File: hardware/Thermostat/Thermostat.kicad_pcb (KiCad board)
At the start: 2 copper layers, 111.2 x 76.5 mm, 47 parts, among them J1 Barrel_Jack_Switch, J2 Conn_01x02_Pin, J3 AVR-ISP-6, J4 MainConnectorr, K1 G6E, K2 G6E, K3 G6E, K4 G6E, SW1 12MM, SW2 12MM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

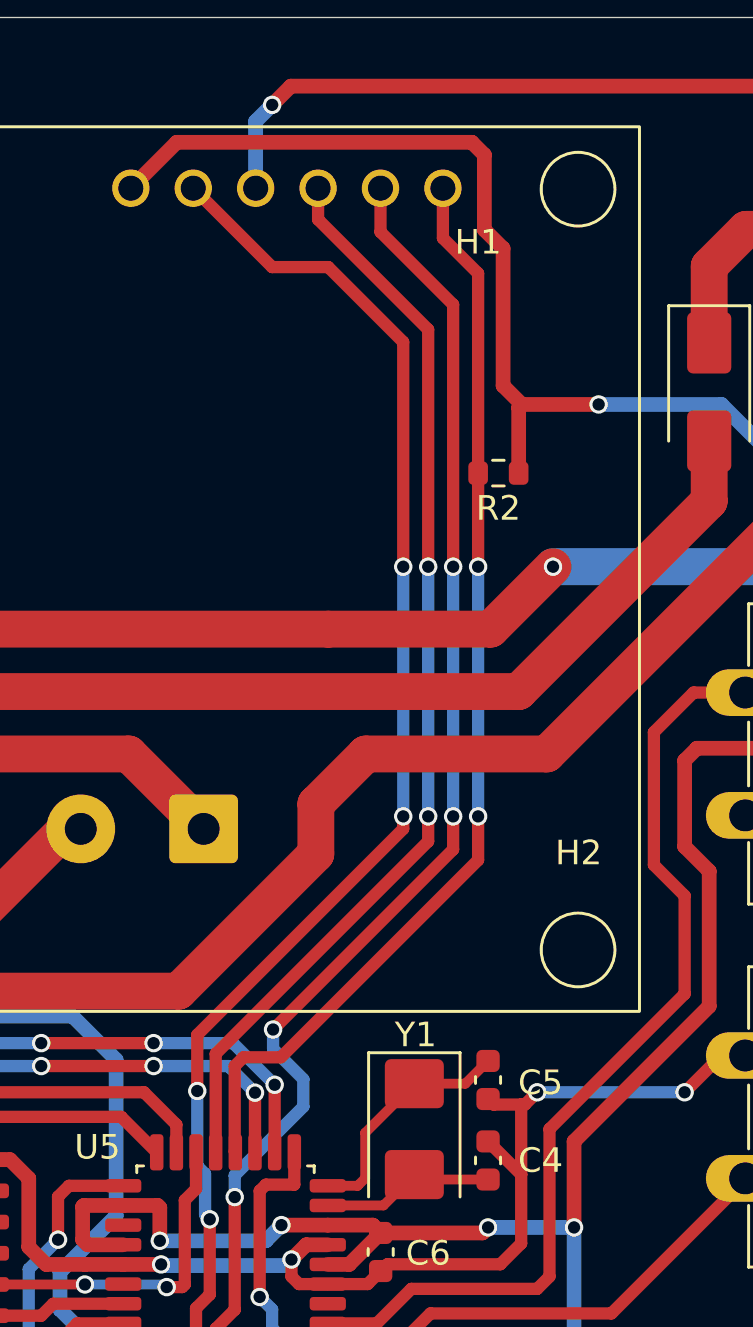
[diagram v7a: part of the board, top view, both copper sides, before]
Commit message: Put switches in order and move resistor
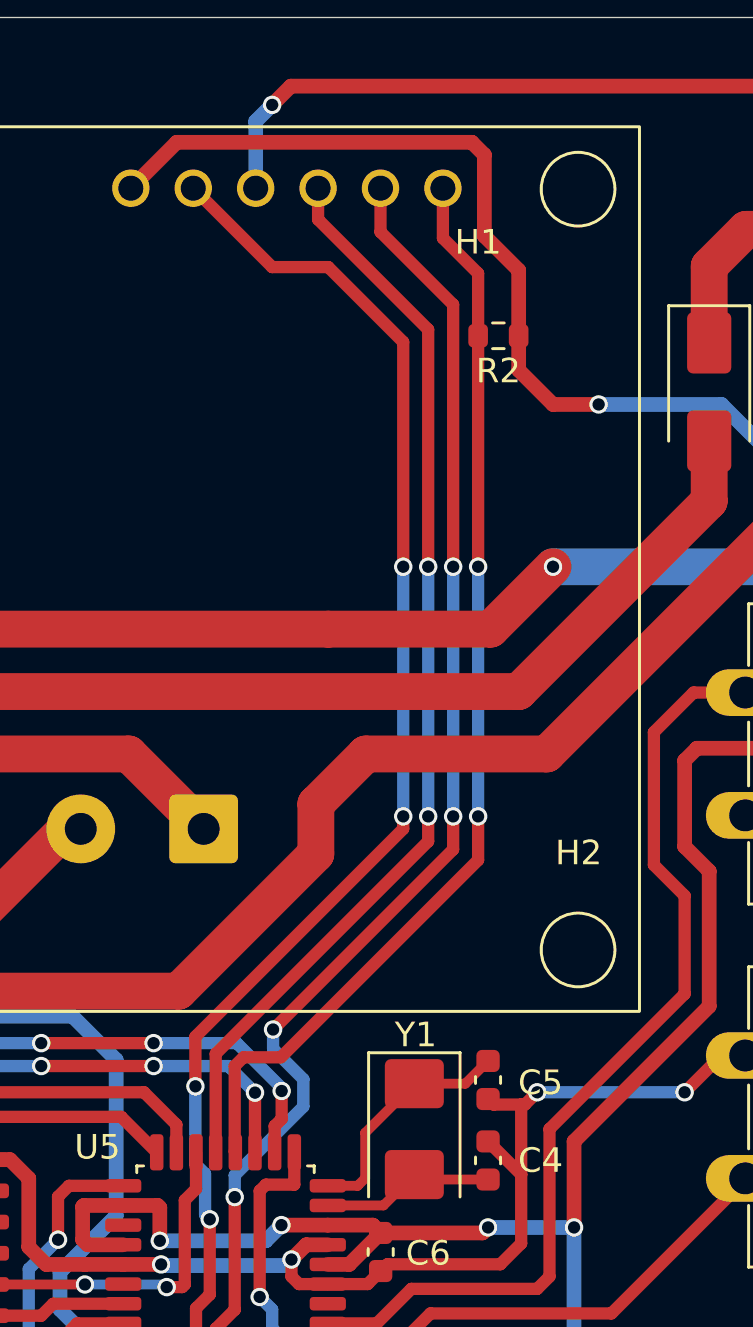
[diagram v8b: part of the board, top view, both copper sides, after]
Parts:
- moved R2 5.59 mm to (197.4, 61.2)
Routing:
- net +5V: track 206.4 -> 202.8 mm
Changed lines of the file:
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@@
 	(footprint "Resistor_SMD:R_0603_1608Metric"
 		(layer "F.Cu")
-		(at 197.421 66.802 180)
+		(at 197.421 61.214 180)
 		(descr "Resistor SMD 0603 (1608 Metric), square (rectangular) end terminal, IPC-7351 nominal, (Body size source: IPC-SM-782 page 72, https://www.pcb-3d.com/wordpress/wp-content/uploads/ipc-sm-782a_amendment_1_and_2.pdf), generated with kicad-footprint-generator")
 		(tags "resistor")
@@
 	)
 	(segment
+		(start 199.644 64.008)
+		(end 201.5 64.008)
+		(width 0.6)
+		(layer "F.Cu")
+		(net 3)
+	)
+	(segment
 		(start 188.5919 97.4059)
 		(end 190.4781 97.4059)
@@
 	)
 	(segment
-		(start 198.246 66.802)
-		(end 198.246 64.136)
-		(width 0.6)
-		(layer "F.Cu")
-		(net 3)
-	)
-	(segment
 		(start 182.1531 98.2059)
 		(end 180.7059 98.2059)
@@
 	)
 	(segment
-		(start 200.5 94)
-		(end 206 88.5)
+		(start 196.85 53.848)
+		(end 196.85 57.15)
 		(width 0.6)
 		(layer "F.Cu")
@@
 	)
 	(segment
-		(start 196.85 53.848)
-		(end 196.85 56.896)
+		(start 200.5 94)
+		(end 206 88.5)
 		(width 0.6)
 		(layer "F.Cu")
@@
 	)
 	(segment
-		(start 197.612 57.658)
-		(end 197.612 63.246)
+		(start 182.463 55.207)
+		(end 184.33 53.34)
 		(width 0.6)
 		(layer "F.Cu")
@@
 	)
 	(segment
+		(start 184.33 53.34)
+		(end 196.342 53.34)
+		(width 0.6)
+		(layer "F.Cu")
+		(net 3)
+	)
+	(segment
 		(start 180.5 96.6559)
 		(end 180.55 96.6059)
@@
 	)
 	(segment
+		(start 196.85 57.15)
+		(end 198.246 58.546)
+		(width 0.6)
+		(layer "F.Cu")
+		(net 3)
+	)
+	(segment
 		(start 190 107.5)
 		(end 191.5 107.5)
@@
 	)
 	(segment
-		(start 211.793 75.989)
-		(end 211.793 68.072)
+		(start 198.246 58.546)
+		(end 198.246 62.61)
 		(width 0.6)
 		(layer "F.Cu")
@@
 	)
 	(segment
-		(start 198.374 64.008)
-		(end 201.5 64.008)
+		(start 211.793 75.989)
+		(end 211.793 68.072)
 		(width 0.6)
 		(layer "F.Cu")
@@
 	)
 	(segment
-		(start 182.463 55.207)
-		(end 184.33 53.34)
-		(width 0.6)
-		(layer "F.Cu")
-		(net 3)
-	)
-	(segment
 		(start 200.5 97.5)
 		(end 200.5 94)
@@
 	)
 	(segment
-		(start 198.246 64.136)
-		(end 198.374 64.008)
-		(width 0.6)
-		(layer "F.Cu")
-		(net 3)
-	)
-	(segment
 		(start 189.5 116.5)
 		(end 191 116.5)
@@
 	)
 	(segment
-		(start 196.85 56.896)
-		(end 197.612 57.658)
-		(width 0.6)
-		(layer "F.Cu")
-		(net 3)
-	)
-	(segment
 		(start 205 82)
 		(end 205 78.5)
@@
 	)
 	(segment
-		(start 197.612 63.246)
-		(end 198.374 64.008)
-		(width 0.6)
-		(layer "F.Cu")
-		(net 3)
-	)
-	(segment
 		(start 209.782 78)
 		(end 211.793 75.989)
@@
 	)
 	(segment
-		(start 184.33 53.34)
-		(end 196.342 53.34)
+		(start 198.246 62.61)
+		(end 199.644 64.008)
 		(width 0.6)
 		(layer "F.Cu")
@@
 	)
 	(segment
+		(start 185.0906 91.757)
+		(end 185.0906 89.7374)
+		(width 0.5)
+		(layer "F.Cu")
+		(net 20)
+	)
+	(segment
 		(start 185.1156 100.791036)
 		(end 185.1156 102.7684)
@@
 	)
 	(segment
+		(start 193.548 81.28)
+		(end 193.548 80.772)
+		(width 0.5)
+		(layer "F.Cu")
+		(net 20)
+	)
+	(segment
 		(start 191.845 110.595)
 		(end 193.75 112.5)
@@
 	)
 	(segment
-		(start 185.1656 89.6624)
-		(end 185.1656 91.948)
-		(width 0.5)
-		(layer "F.Cu")
-		(net 20)
-	)
-	(segment
-		(start 193.548 80.772)
-		(end 193.548 81.28)
-		(width 0.5)
-		(layer "F.Cu")
-		(net 20)
-	)
-	(segment
 		(start 185.1156 105.9684)
 		(end 185.1156 102.7684)
@@
 	)
 	(segment
-		(start 184.912 106.172)
-		(end 185.1156 105.9684)
+		(start 185.0906 89.7374)
+		(end 193.548 81.28)
 		(width 0.5)
 		(layer "F.Cu")
@@
 	)
 	(segment
-		(start 185.166 91.9476)
-		(end 185.1656 91.948)
+		(start 184.912 106.172)
+		(end 185.1156 105.9684)
 		(width 0.5)
 		(layer "F.Cu")
@@
 		(net 20)
 	)
-	(segment
-		(start 193.548 81.28)
-		(end 185.1656 89.6624)
-		(width 0.5)
-		(layer "F.Cu")
-		(net 20)
-	)
 	(via
 		(at 190.5 109)
@@
 	)
 	(via
-		(at 185.1656 91.948)
+		(at 185.0906 91.757)
 		(size 0.75)
 		(drill 0.5)
@@
 	)
 	(segment
-		(start 185.1656 94.9956)
-		(end 185.1656 91.948)
+		(start 185.0906 94.9206)
+		(end 185.0906 91.757)
 		(width 0.5)
 		(layer "B.Cu")
@@
 	)
 	(segment
+		(start 185.483 96.978)
+		(end 185.483 95.313)
+		(width 0.5)
+		(layer "B.Cu")
+		(net 20)
+	)
+	(segment
 		(start 184.912 106.172)
 		(end 186.172 106.172)
@@
 	)
 	(segment
-		(start 185.483 95.313)
-		(end 185.1656 94.9956)
+		(start 185.1656 91.832)
+		(end 185.0906 91.757)
 		(width 0.5)
 		(layer "B.Cu")
@@
 	)
 	(segment
-		(start 185.483 96.978)
-		(end 185.483 95.313)
+		(start 185.483 95.313)
+		(end 185.0906 94.9206)
 		(width 0.5)
 		(layer "B.Cu")
@@
 	)
 	(segment
-		(start 194.564 80.772)
-		(end 194.564 81.788)
-		(width 0.5)
-		(layer "F.Cu")
-		(net 26)
-	)
-	(segment
 		(start 189.738 55.552)
 		(end 190.083 55.207)
@@
 	)
 	(segment
-		(start 194.564 81.788)
-		(end 185.9156 90.4364)
+		(start 194.564 80.772)
+		(end 194.564 81.788)
 		(width 0.5)
 		(layer "F.Cu")
@@
 		(net 26)
 	)
+	(segment
+		(start 194.564 81.788)
+		(end 185.9156 90.4364)
+		(width 0.5)
+		(layer "F.Cu")
+		(net 26)
+	)
 	(via
 		(at 194.564 80.772)
@@
 	)
 	(segment
-		(start 188.3156 91.694)
+		(start 188.3156 93.3704)
 		(end 188.3156 94.4434)
 		(width 0.5)
@@
 	)
 	(segment
+		(start 188.600475 91.948)
+		(end 188.600475 93.085525)
+		(width 0.5)
+		(layer "F.Cu")
+		(net 50)
+	)
+	(segment
 		(start 135.79 113.284)
 		(end 123.29 113.284)
@@
 	)
 	(segment
+		(start 188.600475 93.085525)
+		(end 188.3156 93.3704)
+		(width 0.5)
+		(layer "F.Cu")
+		(net 50)
+	)
+	(segment
 		(start 157.167 109.833)
 		(end 145.501 109.833)
@@
 	)
 	(via
-		(at 188.3156 91.694)
+		(at 188.600475 91.948)
 		(size 0.75)
 		(drill 0.5)
@@
 	)
 	(segment
-		(start 163 98.5)
-		(end 163 104)
+		(start 188.600475 91.826475)
+		(end 186.774 90)
 		(width 0.5)
 		(layer "B.Cu")
@@
 	)
 	(segment
-		(start 188.3156 91.694)
-		(end 186.6216 90)
+		(start 163 98.5)
+		(end 163 104)
 		(width 0.5)
 		(layer "B.Cu")
@@
 	)
 	(segment
+		(start 188.600475 91.948)
+		(end 188.600475 91.826475)
+		(width 0.5)
+		(layer "B.Cu")
+		(net 50)
+	)
+	(segment
 		(start 163 104)
 		(end 161.75 105.25)
@@
 	)
 	(segment
-		(start 186.6216 90)
+		(start 186.774 90)
 		(end 183.388 90)
 		(width 0.5)
